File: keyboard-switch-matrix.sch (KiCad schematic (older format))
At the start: 170 parts

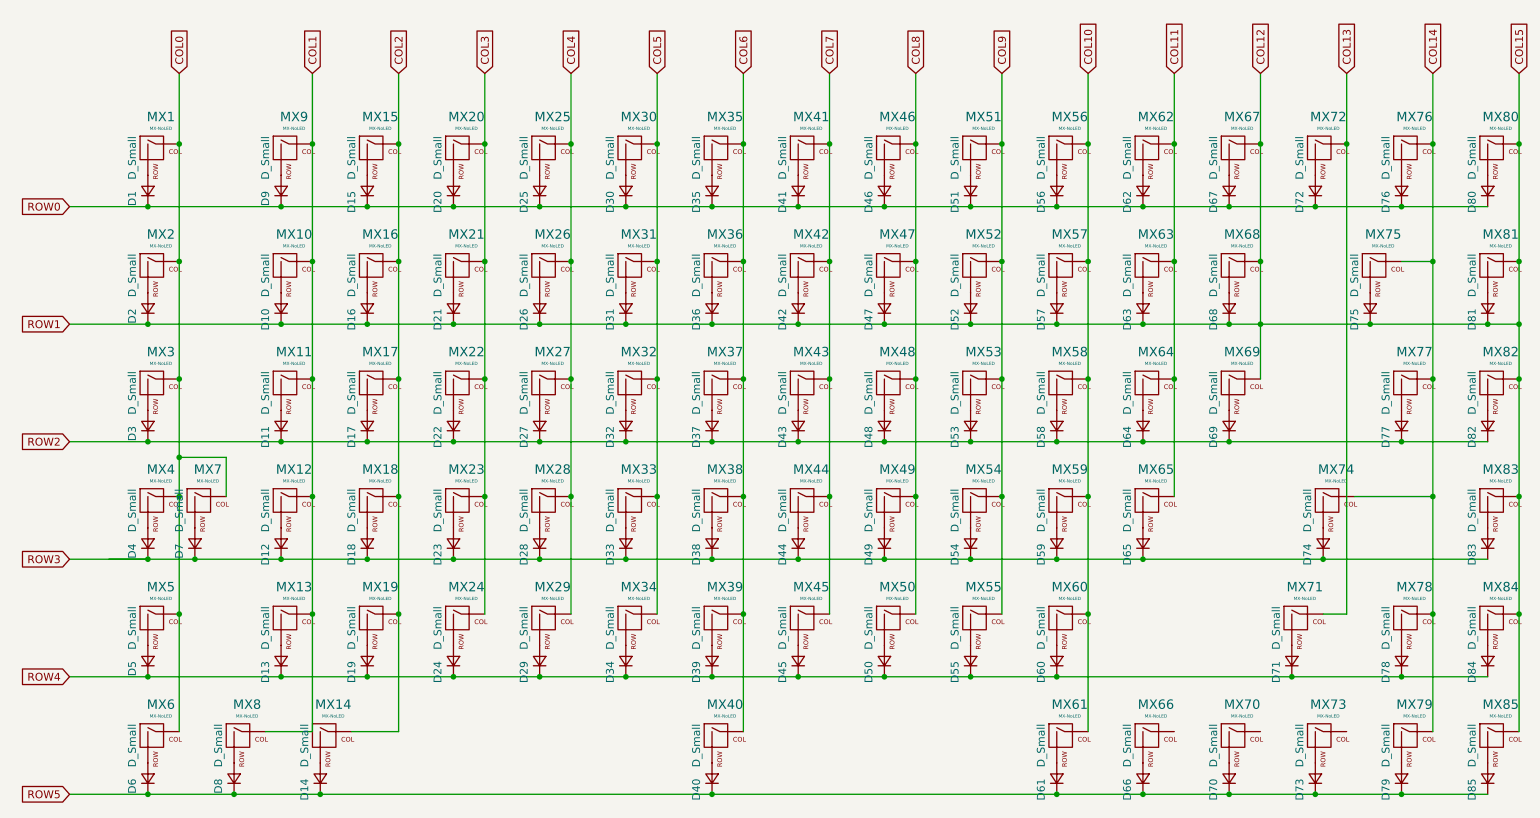
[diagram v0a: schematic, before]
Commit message: initial 75% switch layout, walking back stepped capslock :(
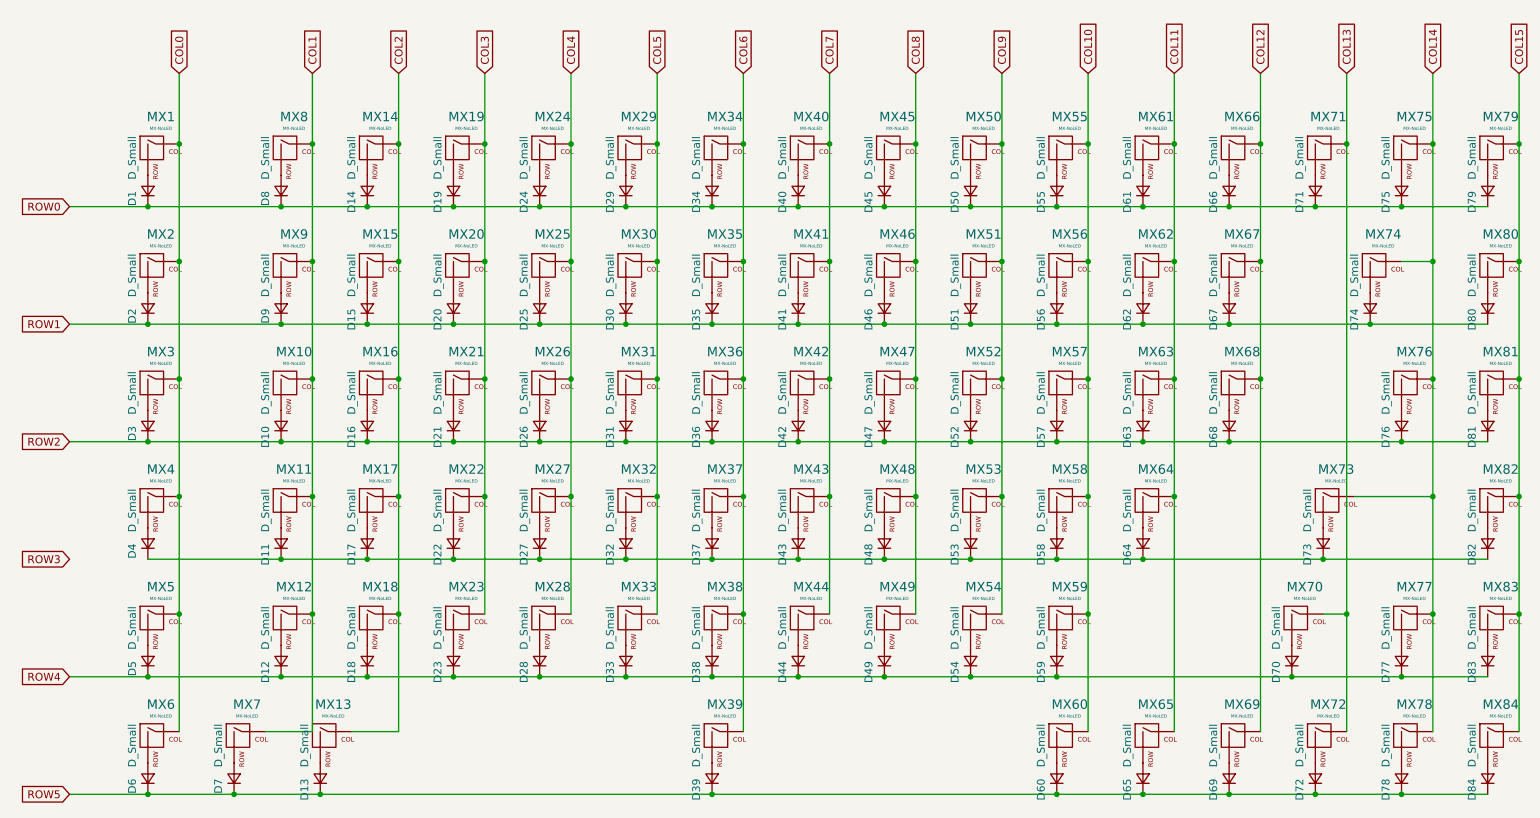
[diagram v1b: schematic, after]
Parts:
- removed D4: D_Small, Diode_SMD:D_SOD-123, symbol Device:D_Small
- removed MX4: MX-NoLED, MX_Only:MXOnly-1U-Hotswap, symbol MX_Alps_Hybrid:MX-NoLED
- MX13: renamed from MX14; footprint MX_Only:MXOnly-1U-Hotswap -> MX_Only:MXOnly-1.25U-Hotswap
- MX3: footprint MX_Only:MXOnly-1U-Hotswap -> MX_Only:MXOnly-1.5U-Hotswap
- MX39: renamed from MX40; footprint MX_Only:MXOnly-1U-Hotswap -> MX_Only:MXOnly-6.25U-Hotswap
- MX4: renamed from MX7; footprint MX_Only:MXOnly-1U-Hotswap -> MX_Only:MXOnly-1.75U-Hotswap
- MX5: footprint MX_Only:MXOnly-1U-Hotswap -> MX_Only:MXOnly-2.25U-Hotswap
- MX6: footprint MX_Only:MXOnly-1U-Hotswap -> MX_Only:MXOnly-1.25U-Hotswap
- MX7: renamed from MX8; footprint MX_Only:MXOnly-1U-Hotswap -> MX_Only:MXOnly-1.25U-Hotswap
- MX70: renamed from MX71; footprint MX_Only:MXOnly-1U-Hotswap -> MX_Only:MXOnly-1.75U-Hotswap
- MX73: renamed from MX74; footprint MX_Only:MXOnly-1U-Hotswap -> MX_Only:MXOnly-2.25U-Hotswap
- MX74: renamed from MX75; footprint MX_Only:MXOnly-1U-Hotswap -> MX_Only:MXOnly-2U-Hotswap
- MX76: renamed from MX77; footprint MX_Only:MXOnly-1U-Hotswap -> MX_Only:MXOnly-1.5U-Hotswap
- renumbered D11 to D10, D12 to D11, D13 to D12, D14 to D13, D15 to D14, D16 to D15, D17 to D16, D18 to D17, D19 to D18, D20 to D19, D21 to D20, D22 to D21, D23 to D22, D24 to D23, D25 to D24, D26 to D25, D27 to D26, D28 to D27, D29 to D28, D30 to D29, D31 to D30, D32 to D31, D33 to D32, D34 to D33, D35 to D34, D36 to D35, D37 to D36, D38 to D37, D39 to D38, D40 to D39, D7 to D4, D41 to D40, D42 to D41, D43 to D42, D44 to D43, D45 to D44, D46 to D45, D47 to D46, D48 to D47, D49 to D48, D50 to D49, D51 to D50, D52 to D51, D53 to D52, D54 to D53, D55 to D54, D56 to D55, D57 to D56, D58 to D57, D59 to D58, D60 to D59, D61 to D60, D62 to D61, D63 to D62, D64 to D63, D65 to D64, D66 to D65, D67 to D66, D68 to D67, D69 to D68, D70 to D69, D8 to D7, D71 to D70, D72 to D71, D73 to D72, D74 to D73, D75 to D74, D76 to D75, D77 to D76, D78 to D77, D79 to D78, D80 to D79, D9 to D8, D81 to D80, D82 to D81, D83 to D82, D84 to D83, D85 to D84, D10 to D9, MX11 to MX10, MX12 to MX11, MX13 to MX12, MX15 to MX14, MX16 to MX15, MX17 to MX16, MX18 to MX17, MX19 to MX18, MX20 to MX19, MX21 to MX20, MX22 to MX21, MX23 to MX22, MX24 to MX23, MX25 to MX24, MX26 to MX25, MX27 to MX26, MX28 to MX27, MX29 to MX28, MX30 to MX29, MX31 to MX30, MX32 to MX31, MX33 to MX32, MX34 to MX33, MX35 to MX34, MX36 to MX35, MX37 to MX36, MX38 to MX37, MX39 to MX38, MX41 to MX40, MX42 to MX41, MX43 to MX42, MX44 to MX43, MX45 to MX44, MX46 to MX45, MX47 to MX46, MX48 to MX47, MX49 to MX48, MX50 to MX49, MX51 to MX50, MX52 to MX51, MX53 to MX52, MX54 to MX53, MX55 to MX54, MX56 to MX55, MX57 to MX56, MX58 to MX57, MX59 to MX58, MX60 to MX59, MX61 to MX60, MX62 to MX61, MX63 to MX62, MX64 to MX63, MX65 to MX64, MX66 to MX65, MX67 to MX66, MX68 to MX67, MX69 to MX68, MX70 to MX69, MX72 to MX71, MX73 to MX72, MX76 to MX75, MX78 to MX77, MX79 to MX78, MX80 to MX79, MX9 to MX8, MX81 to MX80, MX82 to MX81, MX83 to MX82, MX84 to MX83, MX85 to MX84, MX10 to MX9
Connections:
- net COL11: now also MX65.1 (COL)
- net COL12: now also MX69.1 (COL); no longer D15.1 (K), D2.1 (K), D20.1 (K), D25.1 (K), D30.1 (K), D35.1 (K), D41.1 (K), D46.1 (K), D51.1 (K), D56.1 (K), D62.1 (K), D67.1 (K), D74.1 (K), D80.1 (K), D9.1 (K), MX79.1 (COL), MX80.1 (COL), MX81.1 (COL), MX82.1 (COL), MX83.1 (COL), MX84.1 (COL)
- net COL13: now also MX72.1 (COL)
- net ROW3: no longer D11.1 (K), D17.1 (K), D22.1 (K), D27.1 (K), D32.1 (K), D37.1 (K), D4.1 (K), D43.1 (K), D48.1 (K), D53.1 (K), D58.1 (K), D64.1 (K), D73.1 (K), D82.1 (K)
- new net: D11.1 (K), D17.1 (K), D22.1 (K), D27.1 (K), D32.1 (K), D37.1 (K), D4.1 (K), D43.1 (K), D48.1 (K), D53.1 (K), D58.1 (K), D64.1 (K), D73.1 (K), D82.1 (K)
- new net COL15: MX79.1 (COL), MX80.1 (COL), MX81.1 (COL), MX82.1 (COL), MX83.1 (COL), MX84.1 (COL)
- new net ROW1: D15.1 (K), D2.1 (K), D20.1 (K), D25.1 (K), D30.1 (K), D35.1 (K), D41.1 (K), D46.1 (K), D51.1 (K), D56.1 (K), D62.1 (K), D67.1 (K), D74.1 (K), D80.1 (K), D9.1 (K)
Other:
- moved on the sheet: D4, MX4
